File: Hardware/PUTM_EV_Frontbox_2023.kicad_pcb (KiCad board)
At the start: 4 copper layers, 97 x 78 mm, 294 parts, among them IC1 MCP1501T-18E_CHY, J1 Conn_02x16_Counter_Clockwise, J3 M80-5100622, J4 M80-5100622, K1 FINDER-32.21-x000, Q1 NX7002AK, U1 LM4040C33FTA, U10 MCP6001-OT, U11 FODM217B, U12 TLP291-4, U13 TLP291-4, U14 MCP2542FDxMF, U15 MCP6002-xMC, U16 MCP6N11-005, U17 MCP6001, U18 MCP6002-xMC, U19 MCP6N11-005, U2 STM32G473RCTx, U20 MCP6001, U21 MCP6N11-005, U22 MCP6001, U23 MCP6001-OT, U24 AD8226BRMZ-R7, U25 MCP6N11-005, U26 MCP6001, U27 MCP6N11-005, U28 MCP6001, U29 MCP6N11-005, U3 IMS330DHCX, U30 MCP6001, U31 MCP6002-xMC, U32 STLINK-V3MODS, U33 MCP6002-xMC, U34 AD8226BRMZ-R7, U35 AD8226BRMZ-R7, U36 AD8226BRMZ-R7, U37 MCP6001-OT, U4 TLV743P, U5 LM62440-Q1, U6 TLV743P, U7 TLV743P, U8 MCP2542FDxMF, U9 MCP6001-OT, Y1 ABM8G-48.000MHZ

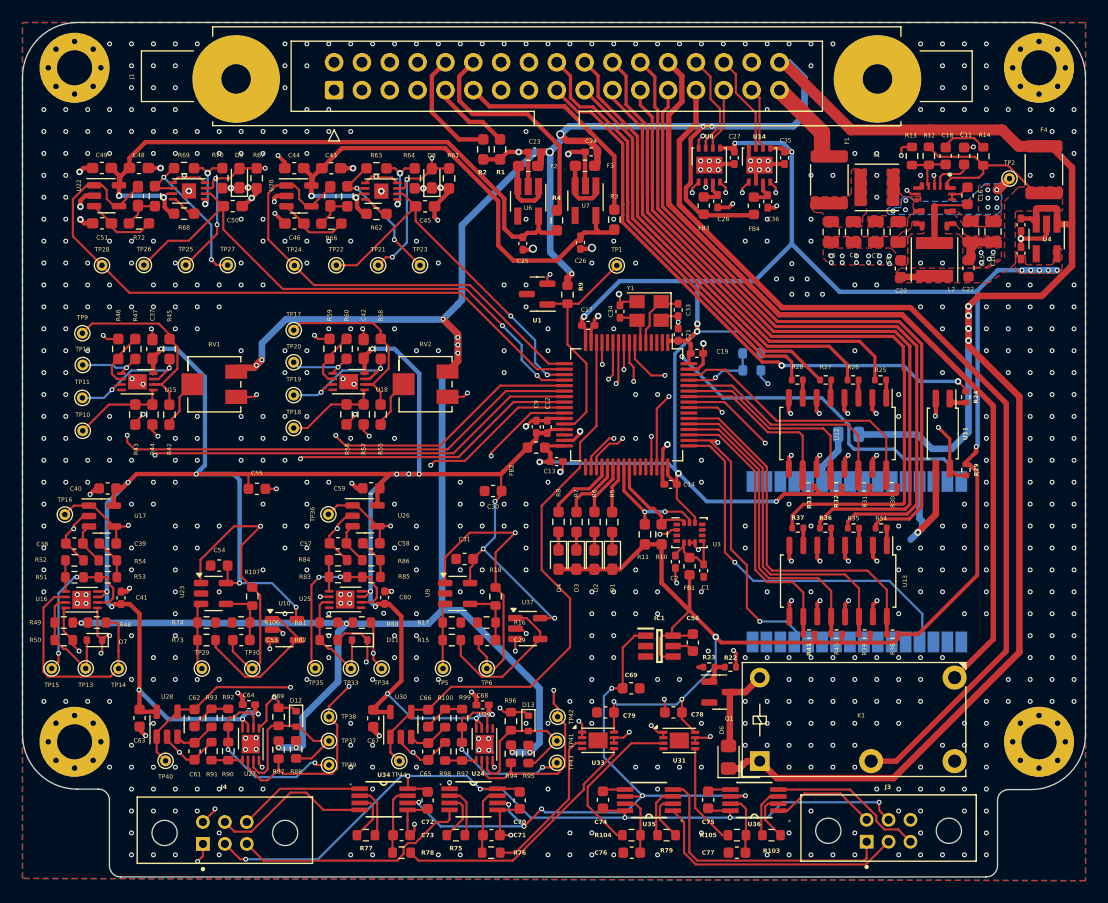
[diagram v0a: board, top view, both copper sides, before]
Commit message: Converter change
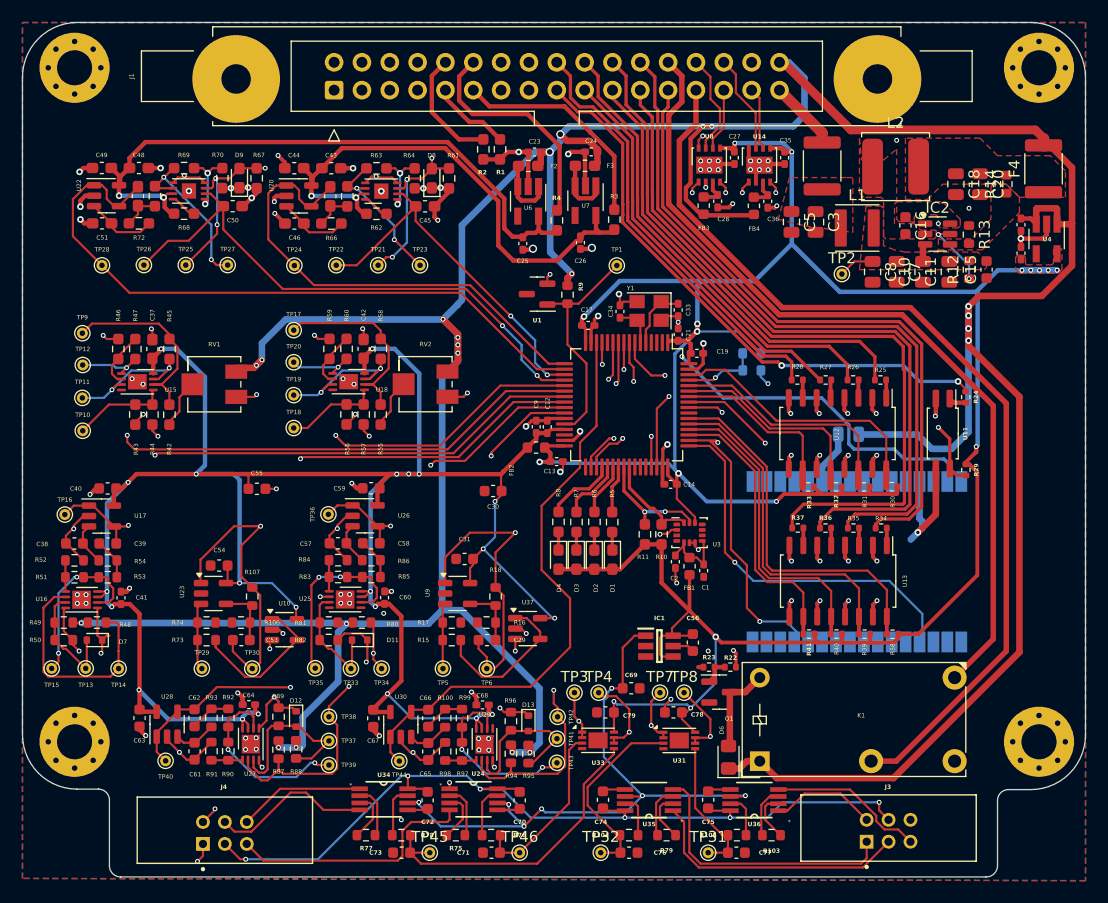
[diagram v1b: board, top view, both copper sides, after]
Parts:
- removed C22: 22u, Capacitor_SMD:C_0603_1608Metric
- removed U5: LM62440-Q1, footprints:IC_LM61460AANRJRR
- added IC2: TPS54202HDDCR, Package_TO_SOT_SMD:SOT-23-6, F.Cu at (219.9, 84.5)
- added TP3: BR_N, TestPoint:TestPoint_THTPad_D1.0mm_Drill0.5mm, F.Cu at (186.8, 126.4)
- added TP31: BR_N, TestPoint:TestPoint_THTPad_D1.0mm_Drill0.5mm, F.Cu at (199.0, 141.0)
- added TP32: BR_N, TestPoint:TestPoint_THTPad_D1.0mm_Drill0.5mm, F.Cu at (189.2, 141.0)
- added TP4: BR_N, TestPoint:TestPoint_THTPad_D1.0mm_Drill0.5mm, F.Cu at (189.0, 126.4)
- added TP45: BR_N, TestPoint:TestPoint_THTPad_D1.0mm_Drill0.5mm, F.Cu at (173.6, 141.0)
- added TP46: BR_N, TestPoint:TestPoint_THTPad_D1.0mm_Drill0.5mm, F.Cu at (181.8, 141.0)
- added TP7: BR_N, TestPoint:TestPoint_THTPad_D1.0mm_Drill0.5mm, F.Cu at (194.6, 126.4)
- added TP8: BR_N, TestPoint:TestPoint_THTPad_D1.0mm_Drill0.5mm, F.Cu at (196.8, 126.4)
- C10: value 220n -> 22uF
- C11: value 1u -> 22uF; footprint Capacitor_SMD:C_0603_1608Metric -> Capacitor_SMD:C_0805_2012Metric
- C15: value 220n -> 100nF; footprint Capacitor_SMD:C_0805_2012Metric -> Capacitor_SMD:C_0603_1608Metric
- C16: value 100n -> 100nF
- C18: value 22p -> 22uF; footprint Capacitor_SMD:C_0603_1608Metric -> Capacitor_SMD:C_0805_2012Metric
- C20: value 22u -> 22uF; footprint Capacitor_SMD:C_0603_1608Metric -> Capacitor_SMD:C_0805_2012Metric
- L2: value 1u5 -> 68uF/1.4A; footprint Inductor_SMD:L_Abracon_ASPI-4030S -> Inductor_SMD:L_TDK_VLS6045EX_VLS6045AF
- R12: value 100k -> 510k
- R13: value 24k9 -> 13.3k
- R14: value 1k -> 100k
- moved TP2 17.6 mm to (211.2, 88.2)
- moved R12 11.0 mm to (222.8, 87.8), turned to 90 degrees
- moved C11 10.7 mm to (221.0, 88.0)
- moved C20 10.5 mm to (223.8, 80.0), turned to -90 degrees
- moved L2 9.19 mm to (216.1, 78.4), turned to 0 degrees
- moved R13 8.86 mm to (222.8, 84.6), turned to -90 degrees
- moved C10 7.37 mm to (218.6, 88.0), turned to 90 degrees
- moved C16 6.28 mm to (217.0, 83.8), turned to -90 degrees
- moved C8 4.33 mm to (214.0, 88.0)
- moved L1 4.11 mm to (212.6, 84.0)
- moved C7 4.10 mm to (216.2, 88.0)
- moved C15 3.76 mm to (224.4, 87.8), turned to 90 degrees
- moved C5 3.73 mm to (206.6, 83.5)
- moved C3 3.58 mm to (208.8, 83.5)
- moved R14 3.30 mm to (226.2, 80.0)
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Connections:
- C10 pad 1: /Power section/VIN -> GND
- C10 pad 2: GND -> Net-(IC2-VIN)
- C11 pad 1: Net-(U5-VCC) -> GND
- C11 pad 2: GND -> Net-(IC2-VIN)
- C15 pad 1: /Power section/VIN -> GND
- C15 pad 2: GND -> Net-(IC2-VIN)
- C16 pad 1: /Power section/SW_5V -> /Power section/BOOT_5V
- C16 pad 2: Net-(U5-CBOOT) -> /Power section/SW_5V
- C18 pad 1: Net-(C18-Pad1) -> /Power section/5V_UNFUSED
- C18 pad 2: /Power section/FB -> GND
- C20 pad 1: /Power section/LF_5V -> /Power section/5V_UNFUSED
- C7 pad 1: /Power section/VIN -> Net-(IC2-VIN)
- C71 pad 1: Net-(U24-VOUT) -> Net-(U33A-+)
- C73 pad 1: Net-(U34-VOUT) -> Net-(U33B-+)
- C76 pad 1: Net-(U35-VOUT) -> Net-(U31A-+)
- C77 pad 1: Net-(U36-VOUT) -> Net-(U31B-+)
- C8 pad 1: /Power section/VIN -> Net-(IC2-VIN)
- F4 pad 1: /Power section/LF_5V -> /Power section/5V_UNFUSED
- L1 pad 2: /Power section/VIN -> Net-(IC2-VIN)
- L2 pad 2: /Power section/LF_5V -> /Power section/5V_UNFUSED
- R12 pad 1: /Power section/LF_5V -> /Power section/EN_5V
- R12 pad 2: /Power section/FB -> Net-(IC2-VIN)
- R13 pad 1: /Power section/FB -> GND
- R13 pad 2: GND -> /Power section/FB_5V
- R14 pad 1: /Power section/LF_5V -> /Power section/FB_5V
- R14 pad 2: Net-(C18-Pad1) -> /Power section/5V_UNFUSED
- TP2 pad 1: /Power section/VIN -> Net-(IC2-VIN)
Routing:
- net /Power section/LF_5V: track 20.1 -> 0.00 mm
- net GND: track 246.3 -> 230.9 mm, vias 723 -> 128
- net /Power section/SW_5V: track 6.52 -> 0.00 mm
- net /Power section/EN_5V: track 0.00 -> 6.28 mm, vias 0 -> 2
- net /Tensometer 2: track 55.9 -> 61.4 mm
- net Net-(U33B-+): track 23.7 -> 28.9 mm
- net /Power section/FB: track 5.14 -> 0.00 mm
- net /Tensometer 4: track 43.0 -> 48.0 mm
- net Net-(IC2-VIN): track 0.00 -> 4.91 mm
- net Net-(C18-Pad1): track 4.23 -> 0.00 mm
- net Net-(U5-VCC): track 3.79 -> 0.00 mm
- net Net-(U31A-+): track 14.6 -> 18.0 mm
- net Net-(U31B-+): track 9.42 -> 12.8 mm
- net /Tensometer 3: track 50.9 -> 54.2 mm
- net /Tensometer 1: track 62.4 -> 65.1 mm
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- added copper zone on F.Cu, net /Power section/5V_UNFUSED
- added copper zone on F.Cu, net /Power section/BOOT_5V
- added copper zone on F.Cu, net /Power section/FB_5V
- added copper zone on F.Cu, net /Power section/SW_5V
- added copper zone on F.Cu, net Net-(IC2-VIN)
- removed copper zone on F.Cu, net /Power section/LF_5V
- removed copper zone on B.Cu, net /Power section/VIN
- removed copper zone on F.Cu, net /Power section/VIN

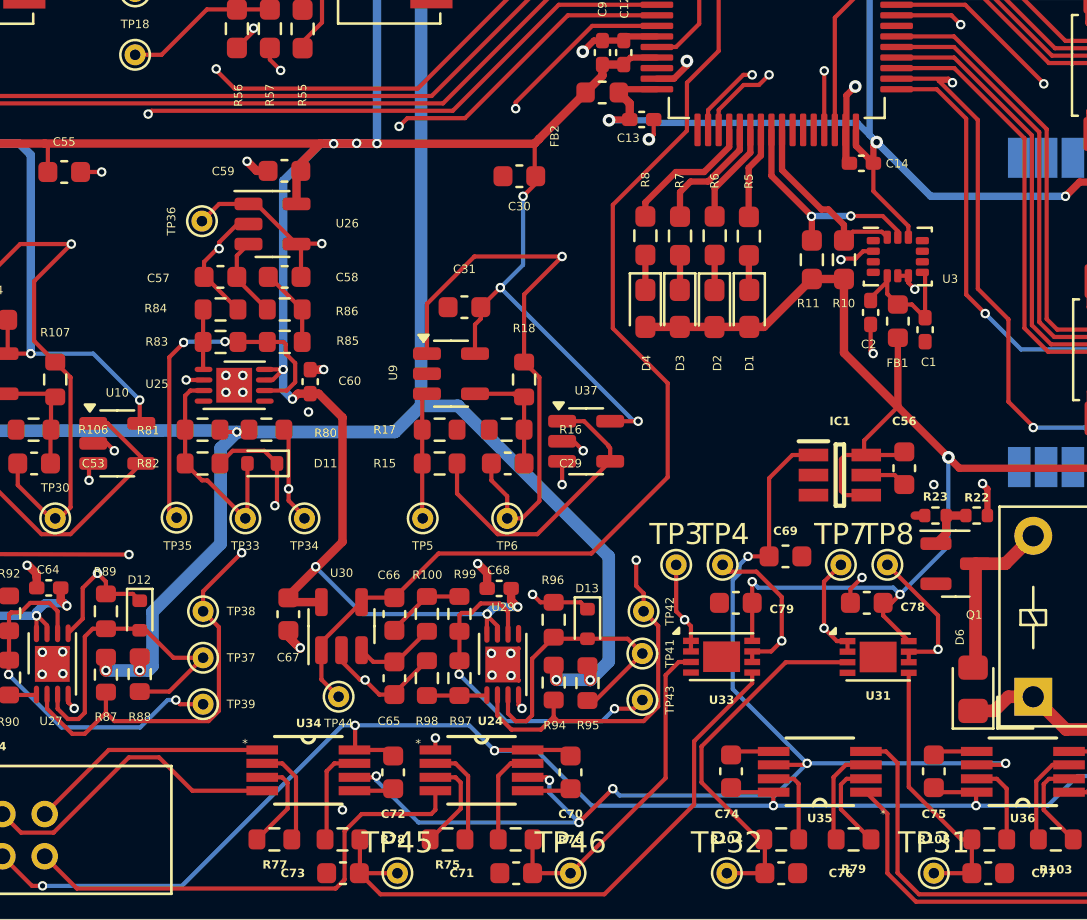
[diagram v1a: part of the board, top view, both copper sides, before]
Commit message: Deleted IMU
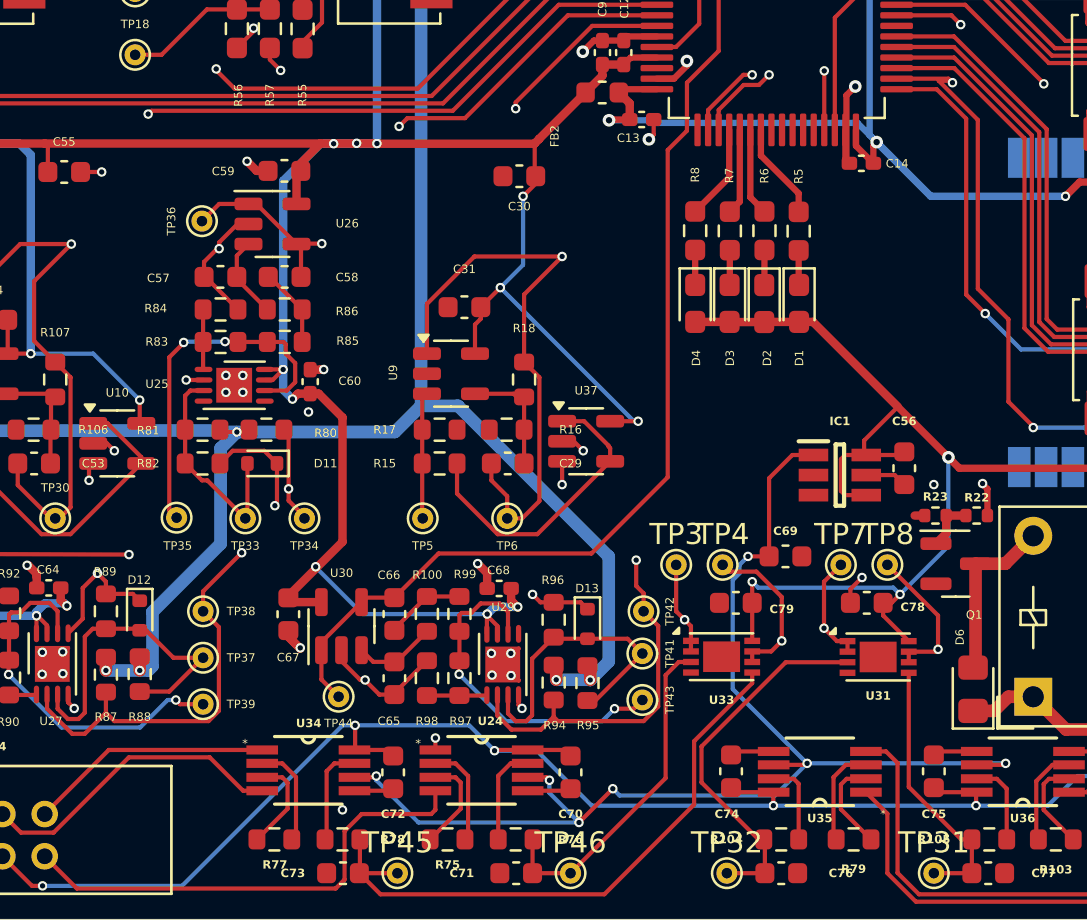
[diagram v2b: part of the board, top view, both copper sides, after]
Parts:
- removed C1, C2: 100nF, Capacitor_SMD:C_0402_1005Metric_Pad0.74x0.62mm_HandSolder
- removed FB1: 60R@100MHz, Inductor_SMD:L_0603_1608Metric
- removed R10, R11: 10k, Resistor_SMD:R_0603_1608Metric_Pad0.98x0.95mm_HandSolder
- removed U3: IMS330DHCX, Package_LGA:LGA-14_3x2.5mm_P0.5mm_LayoutBorder3x4y
- moved D1 2.37 mm to (192.6, 114.0)
- moved D3 2.37 mm to (189.3, 114.0)
- moved R5 2.37 mm to (192.6, 110.6)
- moved D2 2.37 mm to (191.0, 114.0)
- moved R7 2.37 mm to (189.3, 110.6)
- moved D4 2.37 mm to (187.7, 114.0)
- moved R6 2.37 mm to (191.0, 110.6)
- moved R8 2.37 mm to (187.7, 110.6)
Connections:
- U2 pad 40: /IMU_SCL -> unconnected-(U2-PC8-Pad40)
- U2 pad 41: /IMU_SDA -> unconnected-(U2-PC9-Pad41)
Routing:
- net +3.3V: track 260.1 -> 246.5 mm
- net /IMU_SCL: track 10.7 -> 0.00 mm, vias 2 -> 0
- net /IMU_SDA: track 8.97 -> 0.00 mm
- net Net-(U3-VDD): track 7.07 -> 0.00 mm
- net GND: track 230.9 -> 226.5 mm, vias 128 -> 125
- net /GEARBOX_TEMP_2: track 53.5 -> 51.4 mm
- net /DEBUG_LED4: track 6.53 -> 4.53 mm
- net /DEBUG_LED3: track 5.77 -> 4.07 mm
- net /DEBUG_LED2: track 4.80 -> 4.14 mm

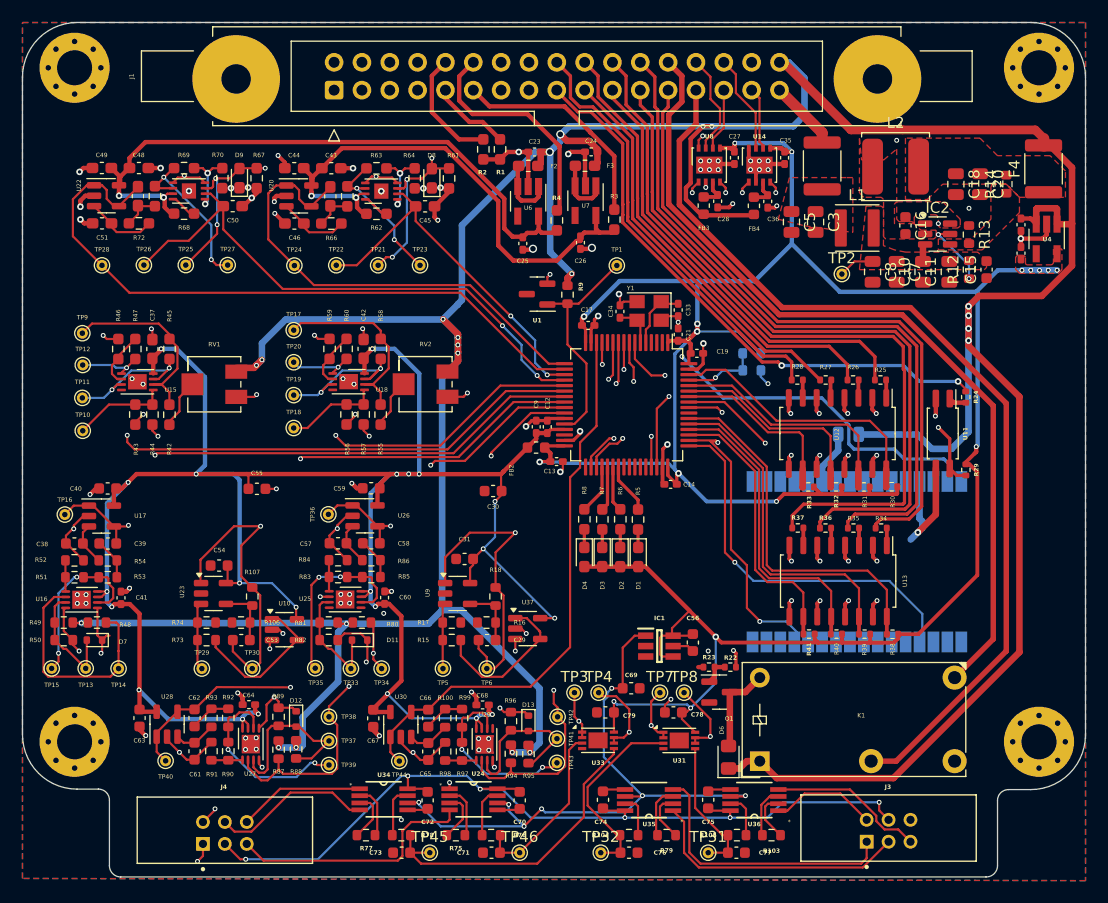
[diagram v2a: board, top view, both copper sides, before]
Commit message: Change voltage followers for tensometer to non iverting ampifiers
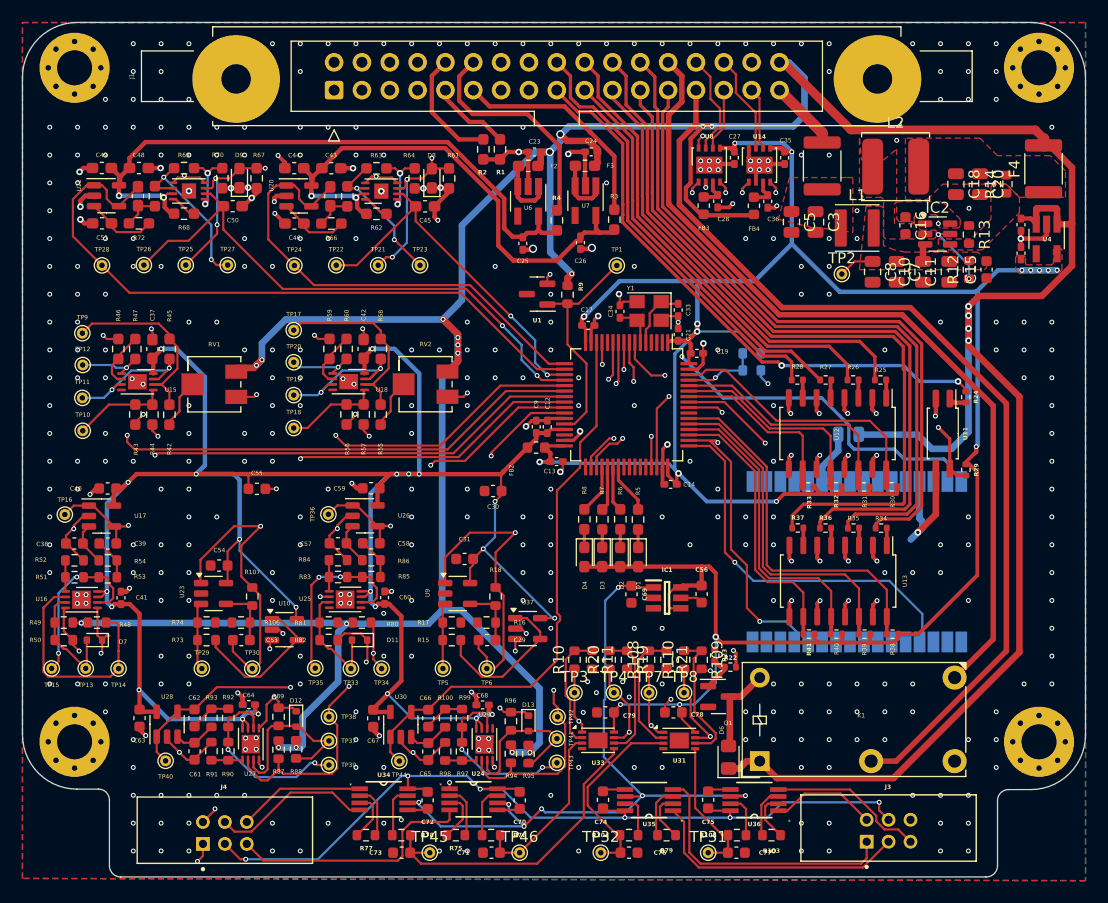
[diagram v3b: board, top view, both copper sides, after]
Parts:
- added R10: 0R, Resistor_SMD:R_0603_1608Metric, F.Cu at (186.8, 123.4)
- added R108: 0R, Resistor_SMD:R_0603_1608Metric, F.Cu at (193.6, 123.4)
- added R109: 0R, Resistor_SMD:R_0603_1608Metric, F.Cu at (198.4, 123.4)
- added R11: 0R, Resistor_SMD:R_0603_1608Metric, F.Cu at (188.4, 123.4)
- added R110: 0R, Resistor_SMD:R_0603_1608Metric, F.Cu at (196.8, 123.4)
- added R19: 0R, Resistor_SMD:R_0603_1608Metric, F.Cu at (191.6, 123.4)
- added R20: 0R, Resistor_SMD:R_0603_1608Metric, F.Cu at (190.0, 123.4)
- added R21: 0R, Resistor_SMD:R_0603_1608Metric, F.Cu at (195.2, 123.4)
- moved C69 8.58 mm to (192.0, 117.4), turned to 90 degrees
- moved C56 4.50 mm to (198.4, 117.4)
- moved IC1 4.46 mm to (195.2, 117.8)
- moved TP4 1.40 mm to (190.4, 126.4)
- moved R23 1.19 mm to (199.6, 123.0), turned to 90 degrees
- moved TP7 1.00 mm to (193.6, 126.4)
- moved Q1 0.42 mm to (199.9, 126.8)
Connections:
- U31 pad 2: /Tensometer 3 -> Net-(U31A--)
- U31 pad 6: /Tensometer 4 -> Net-(U31B--)
- U33 pad 2: /Tensometer 1 -> Net-(U33A--)
- U33 pad 6: /Tensometer 2 -> Net-(U33B--)
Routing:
- net Net-(U31B--): track 0.00 -> 12.8 mm
- net Net-(U33B--): track 0.00 -> 11.8 mm
- net Net-(U31A--): track 0.00 -> 11.3 mm
- net Net-(U33A--): track 0.00 -> 10.8 mm
- net /Tensometers/1,8V: track 58.7 -> 64.3 mm
- net /Tensometer 4: track 48.0 -> 49.7 mm
- net /Tensometer 1: track 65.1 -> 66.8 mm
- net /Tensometer 3: track 54.2 -> 55.7 mm
- net Net-(Q1-G): track 2.46 -> 3.51 mm
- net +3.3V: track 246.5 -> 247.4 mm
- net /Tensometer 2: track 61.8 -> 62.5 mm
- net GND: track 226.5 -> 227.0 mm, vias 125 -> 438
